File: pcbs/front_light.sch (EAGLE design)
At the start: 49 parts, among them IC1 LT3474, IC2 LT3474, IC3 ATTINY24/44/84-SSU

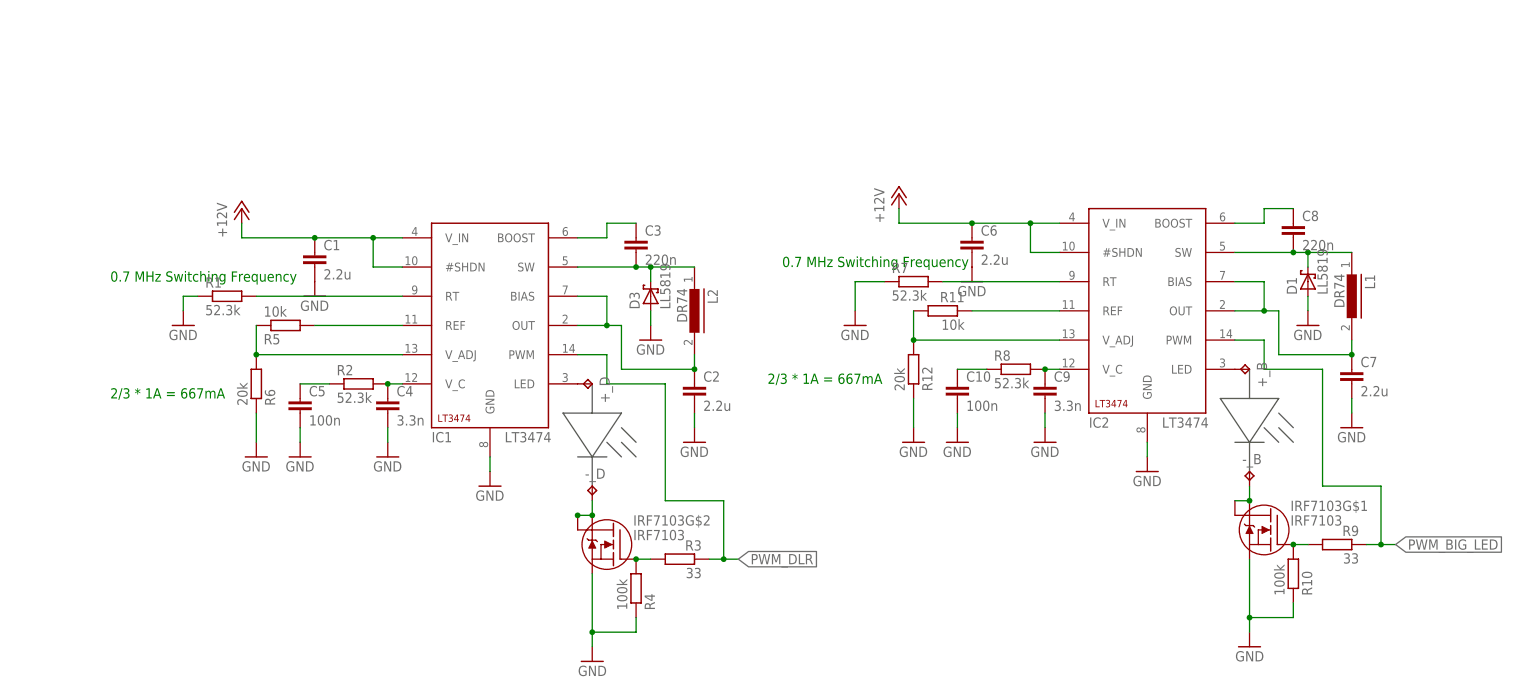
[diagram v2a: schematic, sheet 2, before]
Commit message: FrontLight: use only one LT3474
Since the DLR and the big led will never be used
together they can be driven by a single
led constant current switching IC.
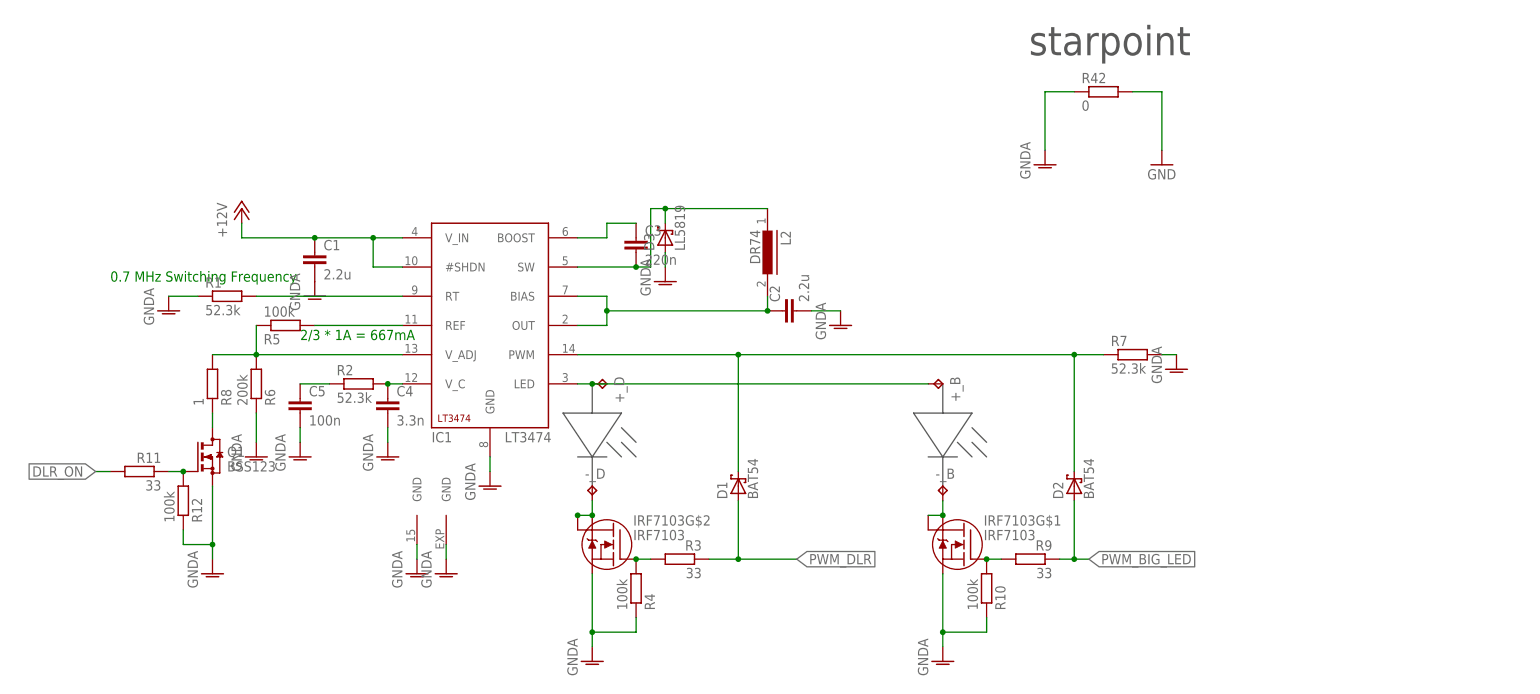
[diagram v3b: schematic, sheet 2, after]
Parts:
- removed C10: 100n, resistor:C-EUC0603
- removed C6, C7: 2.2u, resistor:C-EUC0805
- removed C8: 220n, resistor:C-EUC0603
- removed C9: 3.3n, resistor:C-EUC0603
- removed IC2: LT3474, ltc_swr:LT3474
- removed L1: DR74, inductors:DR74
- removed LOGO2: OSHW_LOGO_10MILX0350-NT, ea:OSHW_LOGO_10MILX0350-NT
- added D2: BAT54, diode:BAT54
- added Q1: BSS123, transistor-small-signal:BSS123
- added R42: 0, rcl:R-EU_R0603
- D1: value LL5819 -> BAT54; device Brunner:DIODESCHOTTKY -> diode:BAT54
- LOGO1: value OSHW_LOGO_6MILX0100-NT -> OSHW_LOGO_6MILX0070-NT; device ea:OSHW_LOGO_6MILX0100-NT -> ea:OSHW_LOGO_6MILX0070-NT
- R11: value 10k -> 33
- R12: value 20k -> 100k
- R5: value 10k -> 100k
- R6: value 20k -> 200k
- R8: value 52.3k -> 1
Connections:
- removed net N$14: IC2G$1.RT, R7.2
- removed net N$16: C8.1, IC2G$1.BOOST
- removed net N$17: C9.1, IC2G$1.V_C, R8.2
- removed net N$18: C10.1, R8.1
- removed net N$19: +_B.TP, IC2G$1.LED
- removed net N$22: IC2G$1.V_ADJ, R11.2, R12.2
- removed net N$27: IC3.(PCINT1/AIN0/ADC1)PA1, SPEED-1.S
- new net DLR_ON: IC3.(PCINT1/AIN0/ADC1)PA1, R11.2
- new net GNDA: C1.2, C2.2, C4.2, C5.2, D3.A, IC1G$1.GND, IC1G$2.GND, IC1G$3.GND, IRF7103G$1.S, IRF7103G$2.S, Q1.S, R1.1, R10.1, R12.1, R4.1, R42.1, R6.1, R7.2
- new net PWM: D1.C, D2.C, IC1G$1.PWM, R7.1
- net +12V: no longer C6.1, IC2G$1.#SHDN, IC2G$1.V_IN
- net GND: now also R42.2; no longer C1.2, C10.2, C2.2, C4.2, C5.2, C6.2, C7.2, C9.2, D1.A, D3.A, IC1G$1.GND, IC2G$1.GND, IRF7103G$1.S, IRF7103G$2.S, R1.1, R10.1, R12.1, R4.1, R6.1, R7.1
- net N$11: now also R8.2
- net N$12: now also IC3.(PCINT9/XTAL2)PB1, SPEED-1.S; no longer C8.2, D1.C, IC2G$1.SW, L1.1
- net N$13: now also Q1.D, R8.1; no longer C7.1, IC2G$1.BIAS, IC2G$1.OUT, L1.2
- net N$15: now also Q1.G, R12.2; no longer IC2G$1.REF
- net N$25: now also IC3.(PCINT8/XTAL1/CLKI)PB0; no longer IC3.(PCINT3/T0/ADC3)PA3
- net N$8: now also +_B.TP
- net PWM_BIG_LED: now also D2.A; no longer IC2G$1.PWM
- net PWM_DLR: now also D1.A; no longer IC1G$1.PWM
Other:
- note added: "starpoint"
- moved on the sheet: +_B, +_D, -_B, C2, D1, D3, IRF7103G$1, L2, LED1, R10, R11, R12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

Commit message: Pcbs: latest changes
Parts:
- removed LOGO1: OSHW_LOGO_6MILX0070-NT, ea:OSHW_LOGO_6MILX0070-NT
- added LOGO2: OSHW_LOGO_6MILX0150-NT, ea:OSHW_LOGO_6MILX0150-NT
- renumbered IC1 to LT3474, IC3 to ATTINY24
